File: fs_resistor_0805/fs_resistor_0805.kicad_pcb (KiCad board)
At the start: 2 copper layers, 15 x 5 mm, 3 parts

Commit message: reorganize the repo
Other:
- board size 15 x 5 mm -> 14 x 4 mm
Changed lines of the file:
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@@
 			(outputformat 1)
 			(mirror no)
-			(drillshape 1)
+			(drillshape 0)
 			(scaleselection 1)
-			(outputdirectory "")
+			(outputdirectory "manufacturing/")
 		)
 	)
@@
 	)
 	(gr_line
-		(start 114 57.5)
-		(end 124 57.5)
+		(start 114 58)
+		(end 124 58)
 		(stroke
 			(width 0.05)
@@
 	)
 	(gr_arc
-		(start 114 62.5)
-		(mid 111.5 60)
-		(end 114 57.5)
+		(start 114 62)
+		(mid 112 60)
+		(end 114 58)
 		(stroke
 			(width 0.05)
@@
 	)
 	(gr_line
-		(start 114 62.5)
-		(end 124 62.5)
+		(start 114 62)
+		(end 124 62)
 		(stroke
 			(width 0.05)
@@
 	)
 	(gr_arc
-		(start 124 57.5)
-		(mid 126.5 60)
-		(end 124 62.5)
+		(start 124 58)
+		(mid 126 60)
+		(end 124 62)
 		(stroke
 			(width 0.05)

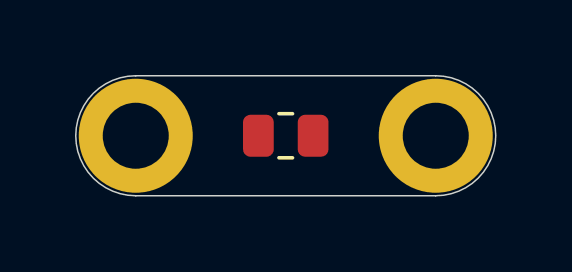
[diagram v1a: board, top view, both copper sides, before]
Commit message: first draft of 0805 breakout board
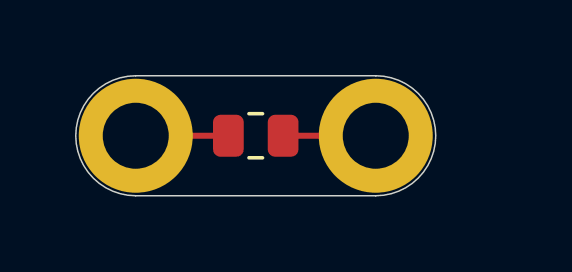
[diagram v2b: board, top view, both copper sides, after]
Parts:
- moved H2 2.00 mm to (122.0, 60.0)
- moved R1 1.00 mm to (118.0, 60.0)
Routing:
- net Net-(H2-Pad1): track 0.00 -> 3.09 mm
- net Net-(H1-Pad1): track 0.00 -> 3.09 mm
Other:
- board size 14 x 4 mm -> 12 x 4 mm
- board text added: "0805"
- board text added: "@flicker stitch"
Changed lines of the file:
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@@
 	(footprint "MountingHole:MountingHole_2.2mm_M2_DIN965_Pad"
 		(layer "F.Cu")
-		(at 124 60)
+		(at 122 60)
 		(descr "Mounting Hole 2.2mm, M2, generated by kicad-footprint-generator mountinghole.py")
 		(tags "mountinghole M2 DIN965")
@@
 	(footprint "Resistor_SMD:R_0805_2012Metric"
 		(layer "F.Cu")
-		(at 119 60)
+		(at 118 60)
 		(descr "Resistor SMD 0805 (2012 Metric), square (rectangular) end terminal, IPC-7351 nominal, (Body size source: IPC-SM-782 page 72, https://www.pcb-3d.com/wordpress/wp-content/uploads/ipc-sm-782a_amendment_1_and_2.pdf)")
 		(tags "resistor")
@@
 	(gr_line
 		(start 114 58)
-		(end 124 58)
+		(end 122 58)
 		(stroke
 			(width 0.05)
@@
 	(gr_line
 		(start 114 62)
-		(end 124 62)
+		(end 122 62)
 		(stroke
 			(width 0.05)
@@
 	)
 	(gr_arc
-		(start 124 58)
-		(mid 126 60)
-		(end 124 62)
+		(start 122 58)
+		(mid 124 60)
+		(end 122 62)
 		(stroke
 			(width 0.05)
@@
 		(layer "Edge.Cuts")
 	)
+	(gr_text "@flicker\nstitch"
+		(at 118 61.75 0)
+		(layer "B.SilkS")
+		(effects
+			(font
+				(size 0.7 0.7)
+			)
+			(justify bottom mirror)
+		)
+	)
+	(gr_text "0805"
+		(at 118 59.5 0)
+		(layer "B.SilkS")
+		(effects
+			(font
+				(size 0.9 0.9)
+			)
+			(justify bottom mirror)
+		)
+	)
+	(segment
+		(start 117.0875 60)
+		(end 114 60)
+		(width 0.2)
+		(layer "F.Cu")
+		(net "Net-(H1-Pad1)")
+	)
+	(segment
+		(start 118.9125 60)
+		(end 122 60)
+		(width 0.2)
+		(layer "F.Cu")
+		(net "Net-(H2-Pad1)")
+	)
 	(embedded_fonts no)

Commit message: add hand soldering pad
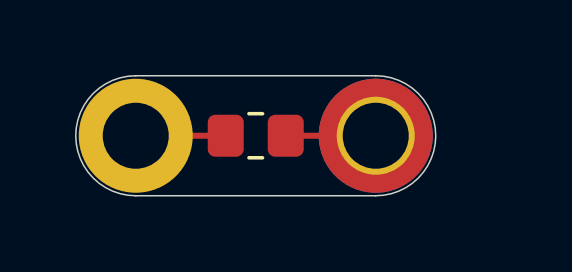
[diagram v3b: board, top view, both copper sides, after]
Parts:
- H2: footprint MountingHole:MountingHole_2.2mm_M2_DIN965_Pad -> MountingHole:MountingHole_2.2mm_M2_DIN965_Pad_TopBottom
- R1: footprint Resistor_SMD:R_0805_2012Metric -> Resistor_SMD:R_0805_2012Metric_Pad1.20x1.40mm_HandSolder
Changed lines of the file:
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@@
 		(property ki_fp_filters "MountingHole*Pad*")
 		(sheetname "/")
-		(sheetfile "flicker_stitch.kicad_sch")
+		(sheetfile "fs_resistor_0805.kicad_sch")
 		(units
 			(unit
@@
 		(embedded_fonts no)
 	)
-	(footprint "MountingHole:MountingHole_2.2mm_M2_DIN965_Pad"
+	(footprint "MountingHole:MountingHole_2.2mm_M2_DIN965_Pad_TopBottom"
 		(layer "F.Cu")
 		(at 122 60)
@@
 		(property ki_fp_filters "MountingHole*Pad*")
 		(sheetname "/")
-		(sheetfile "flicker_stitch.kicad_sch")
+		(sheetfile "fs_resistor_0805.kicad_sch")
 		(units
 			(unit
@@
 		(pad "1" thru_hole circle
 			(at 0 0)
-			(size 3.8 3.8)
+			(size 2.6 2.6)
 			(drill 2.2)
 			(layers "*.Cu" "*.Mask")
@@
 			(zone_connect 2)
 		)
+		(pad "1" connect circle
+			(at 0 0)
+			(size 3.8 3.8)
+			(layers "F.Cu" "F.Mask")
+			(net "Net-(H2-Pad1)")
+			(pinfunction "1_1")
+			(pintype "input")
+			(zone_connect 2)
+		)
+		(pad "1" connect circle
+			(at 0 0)
+			(size 3.8 3.8)
+			(layers "B.Cu" "B.Mask")
+			(net "Net-(H2-Pad1)")
+			(pinfunction "1_1")
+			(pintype "input")
+			(zone_connect 2)
+		)
 		(embedded_fonts no)
 	)
-	(footprint "Resistor_SMD:R_0805_2012Metric"
+	(footprint "Resistor_SMD:R_0805_2012Metric_Pad1.20x1.40mm_HandSolder"
 		(layer "F.Cu")
 		(at 118 60)
-		(descr "Resistor SMD 0805 (2012 Metric), square (rectangular) end terminal, IPC-7351 nominal, (Body size source: IPC-SM-782 page 72, https://www.pcb-3d.com/wordpress/wp-content/uploads/ipc-sm-782a_amendment_1_and_2.pdf)")
-		(tags "resistor")
+		(descr "Resistor SMD 0805 (2012 Metric), square (rectangular) end terminal, IPC-7351 nominal with elongated pad for handsoldering. (Body size source: IPC-SM-782 page 72, https://www.pcb-3d.com/wordpress/wp-content/uploads/ipc-sm-782a_amendment_1_and_2.pdf)")
+		(tags "resistor handsolder")
 		(property "Reference" "R1"
 			(at 0 -1.65 0)
@@
 		(property ki_fp_filters "R_*")
 		(sheetname "/")
-		(sheetfile "flicker_stitch.kicad_sch")
+		(sheetfile "fs_resistor_0805.kicad_sch")
 		(units
 			(unit
@@
 		)
 		(fp_rect
-			(start -1.68 -0.95)
-			(end 1.68 0.95)
+			(start -1.85 -0.95)
+			(end 1.85 0.95)
 			(stroke
 				(width 0.05)
@@
 		)
 		(pad "1" smd roundrect
-			(at -0.9125 0)
-			(size 1.025 1.4)
+			(at -1 0)
+			(size 1.2 1.4)
 			(layers "F.Cu" "F.Mask" "F.Paste")
-			(roundrect_rratio 0.243902)
+			(roundrect_rratio 0.208333)
 			(net "Net-(H1-Pad1)")
 			(pintype "passive")
 		)
 		(pad "2" smd roundrect
-			(at 0.9125 0)
-			(size 1.025 1.4)
+			(at 1 0)
+			(size 1.2 1.4)
 			(layers "F.Cu" "F.Mask" "F.Paste")
-			(roundrect_rratio 0.243902)
+			(roundrect_rratio 0.208333)
 			(net "Net-(H2-Pad1)")
 			(pintype "passive")

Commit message: add plus sign on resistor boards
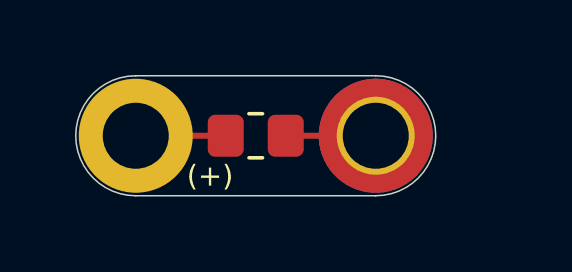
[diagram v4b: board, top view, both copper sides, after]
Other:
- board text added: "(+)"
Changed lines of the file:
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@@
 		(layer "Edge.Cuts")
+	)
+	(gr_text "(+)"
+		(at 115.7 61.75 0)
+		(layer "F.SilkS")
+		(effects
+			(font
+				(size 0.7 0.7)
+			)
+			(justify left bottom)
+		)
 	)
 	(gr_text "@flicker\nstitch"
